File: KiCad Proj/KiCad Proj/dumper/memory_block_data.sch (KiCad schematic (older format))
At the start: 6 parts, among them U1 74HC595, U2 SN74LVC8T245PWR, U3 74HC595, U4 SN74LVC8T245PWR, U5 SN74LVC8T245PWR

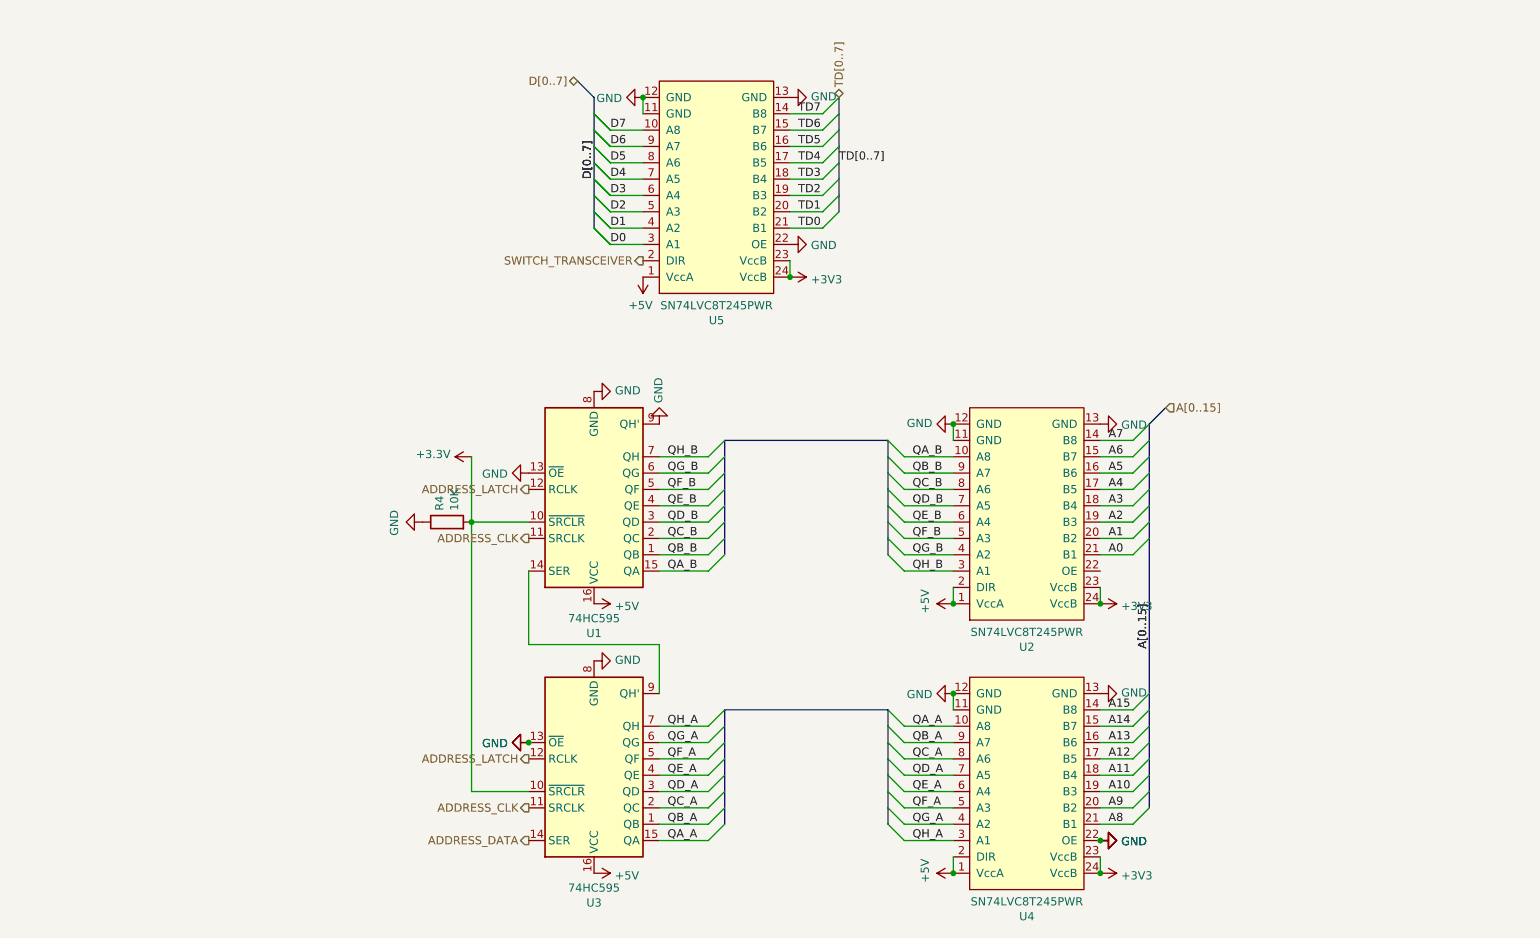
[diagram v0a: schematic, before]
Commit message: Fixed up the schematic and PCB for two very severe omissions
I forgot to translate the WR, RD, and CS pins and added a transceiver for those

I also forgot that the transceivers should have CART_VCC on VccB
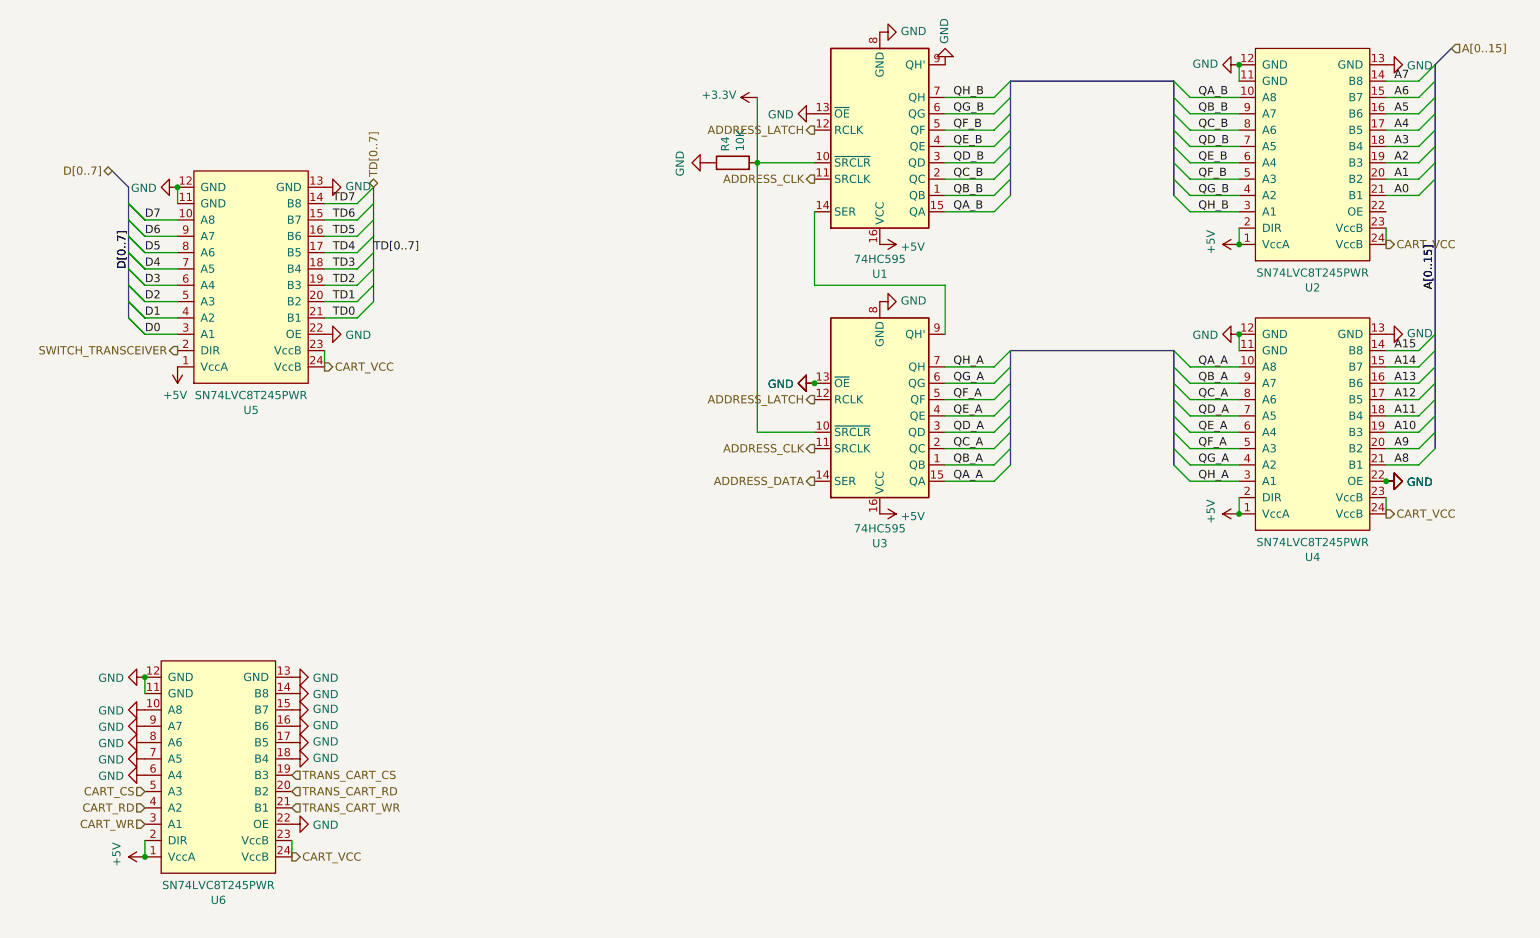
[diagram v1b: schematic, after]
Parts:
- added U6: SN74LVC8T245PWR, Package_SO:TSSOP-24_6.1x7.8mm_P0.65mm, symbol DumperICs:SN74LVC8T245PWR
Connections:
- net +3V3: no longer U2.23 (VccB), U2.24 (VccB), U4.23 (VccB), U4.24 (VccB), U5.23 (VccB), U5.24 (VccB)
- net +5V: now also U6.1 (VccA), U6.2 (DIR)
- net GND: now also U6.10 (A8), U6.11 (GND), U6.12 (GND), U6.13 (GND), U6.14 (B8), U6.15 (B7), U6.16 (B6), U6.17 (B5), U6.18 (B4), U6.22 (OE), U6.6 (A4), U6.7 (A5), U6.8 (A6), U6.9 (A7)
- new net CART_CS: U6.5 (A3)
- new net CART_RD: U6.4 (A2)
- new net CART_VCC: U2.23 (VccB), U2.24 (VccB), U4.23 (VccB), U4.24 (VccB), U5.23 (VccB), U5.24 (VccB), U6.23 (VccB), U6.24 (VccB)
- new net CART_WR: U6.3 (A1)
- new net TRANS_CART_CS: U6.19 (B3)
- new net TRANS_CART_RD: U6.20 (B2)
- new net TRANS_CART_WR: U6.21 (B1)
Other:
- moved on the sheet: R4, U1, U2, U3, U4, U5
